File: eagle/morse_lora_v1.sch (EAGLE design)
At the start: 20 parts

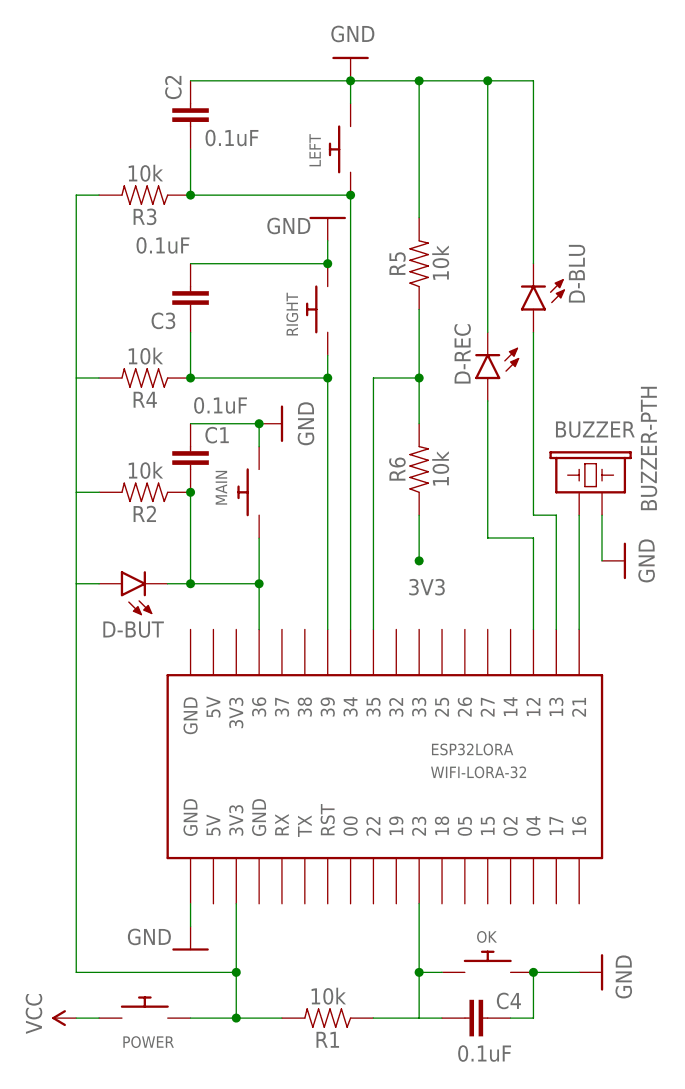
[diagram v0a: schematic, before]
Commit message: add power icon
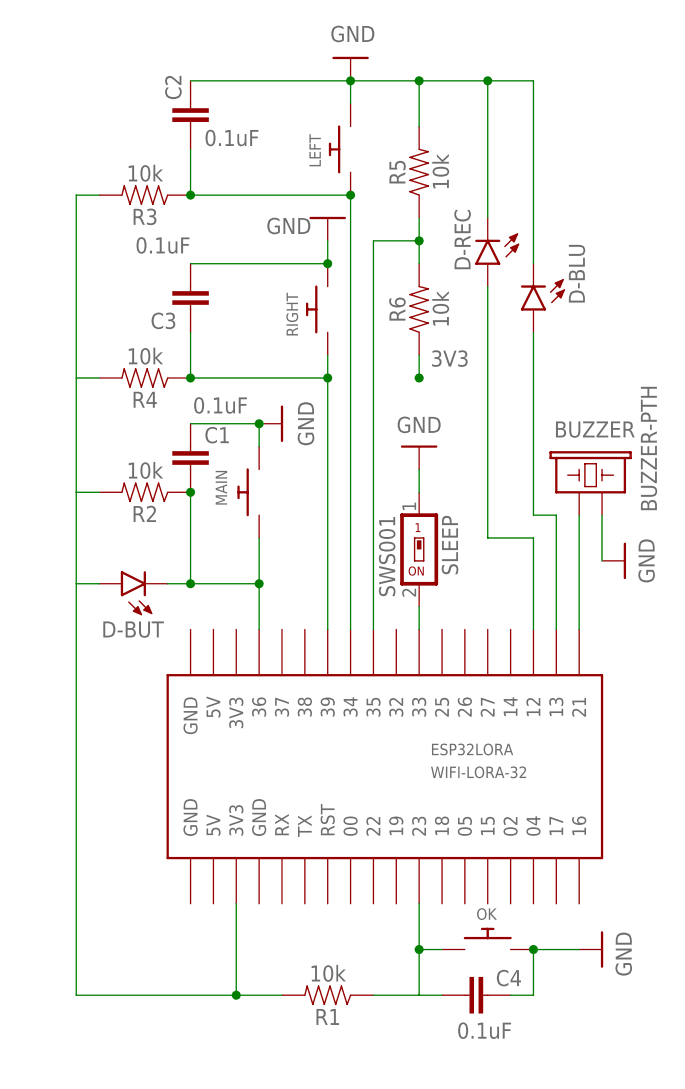
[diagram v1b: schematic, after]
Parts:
- removed POWER: (no value), adafruit:SWITCH_PUSHBUTTONEVQ-PE
- added SLEEP: SWS001, smd-special:SWS001
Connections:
- removed net VCC: POWER.P$1
- new net N$13: ESP32LORA.33, SLEEP.2
- net 3V3@1: no longer POWER.P$2
- net GND: now also SLEEP.1; no longer ESP32LORA.GND@1
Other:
- moved on the sheet: C4, D-REC, OK, R1, R5, R6
